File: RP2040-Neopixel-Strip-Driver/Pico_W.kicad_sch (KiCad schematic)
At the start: 1 part

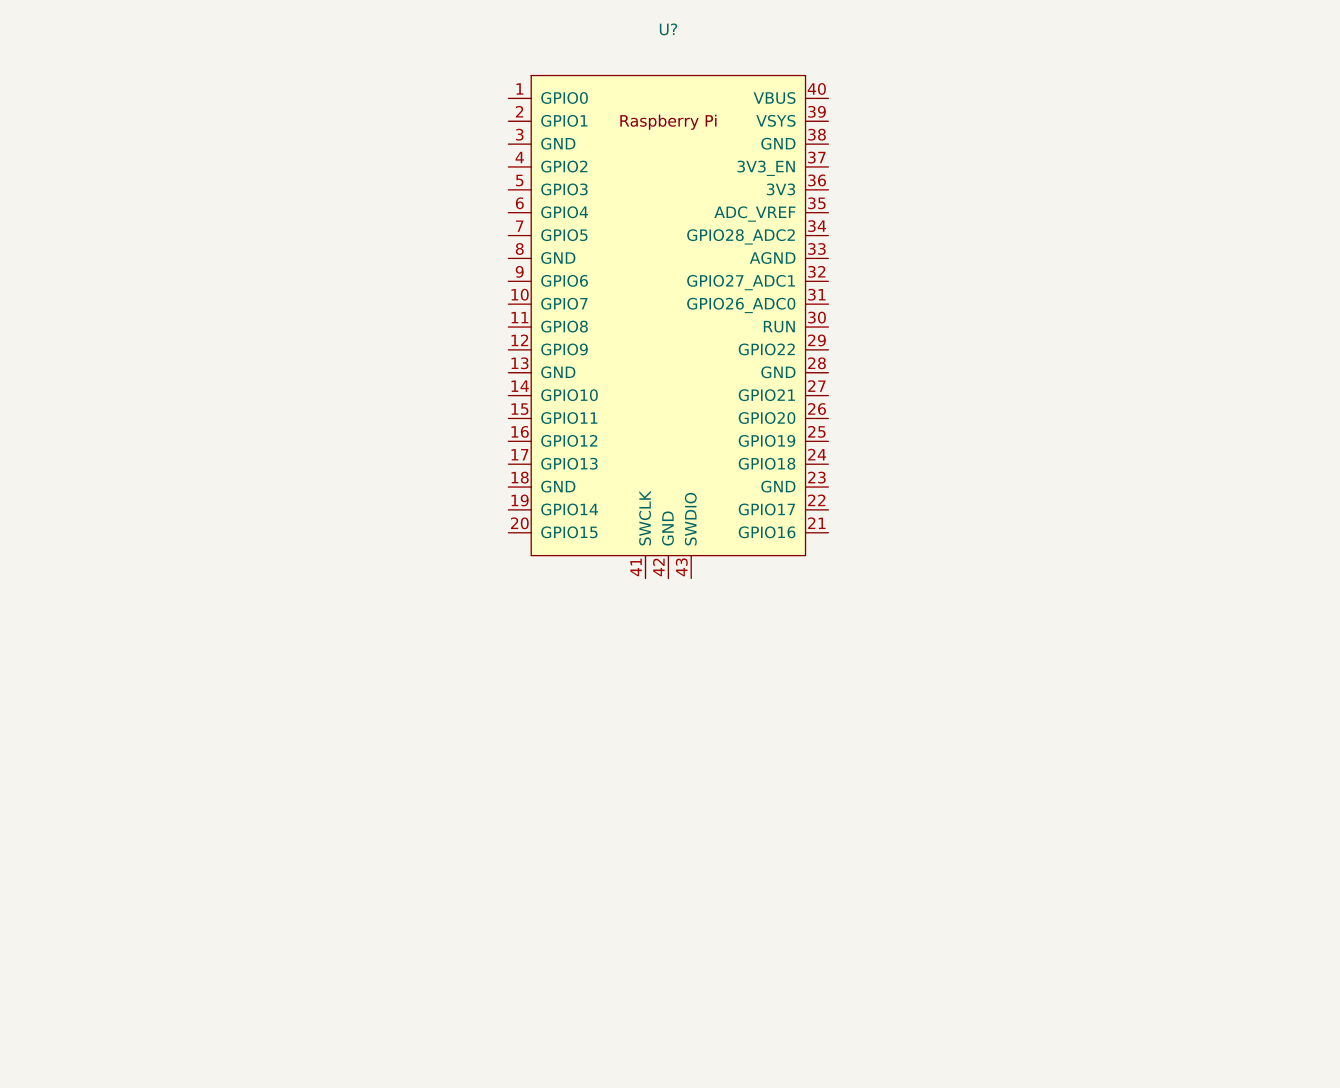
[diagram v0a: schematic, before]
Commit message: Removed RP2040 Schematic, Going with Pico W Module
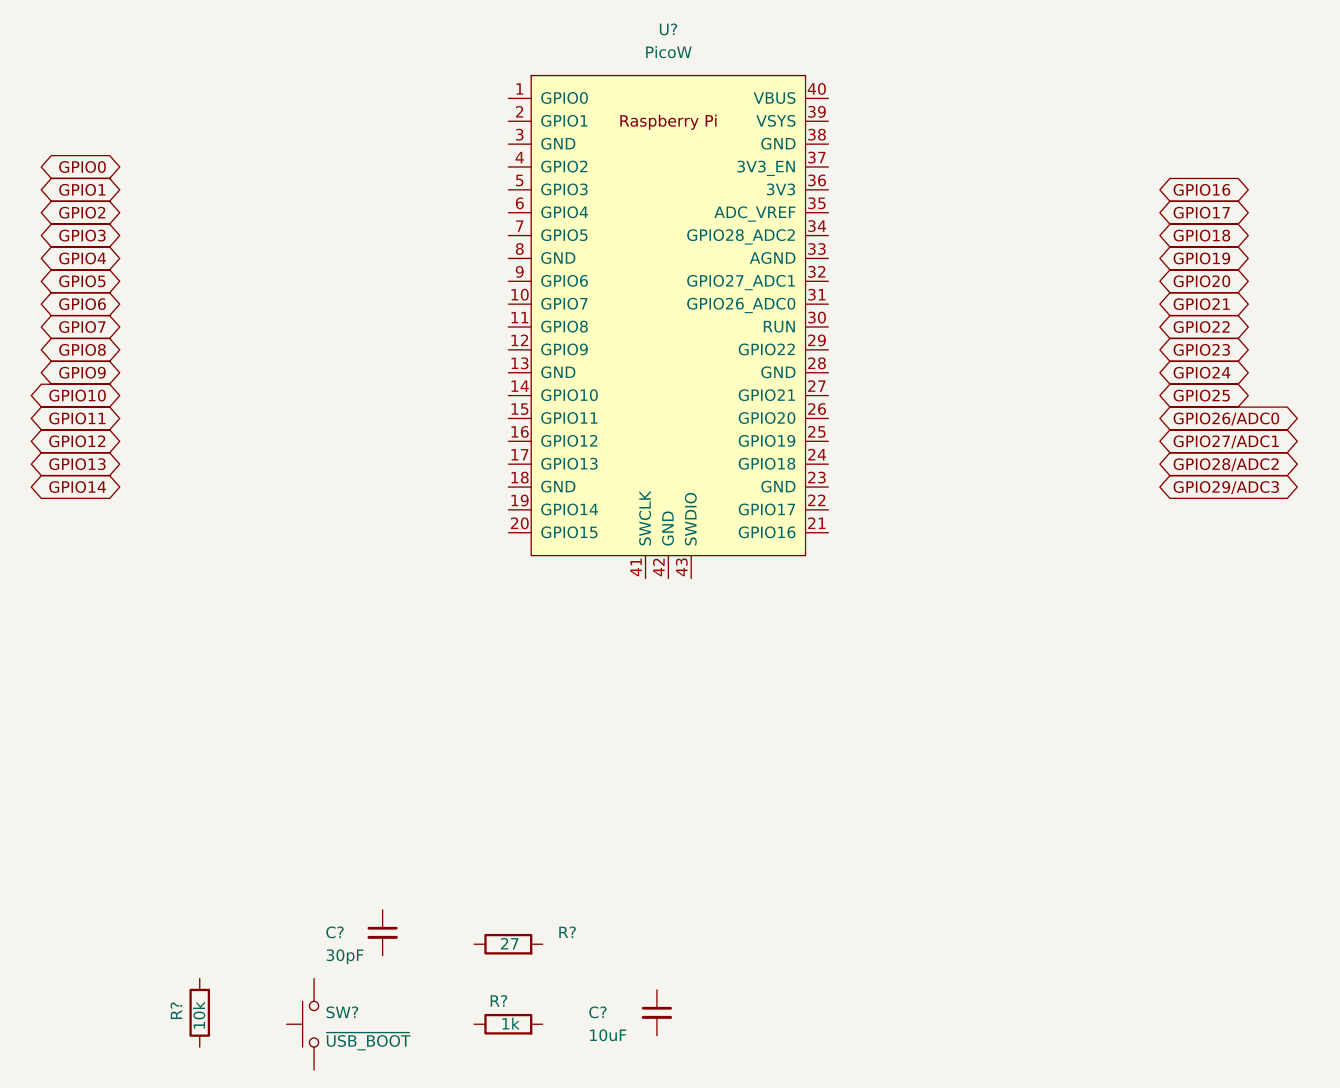
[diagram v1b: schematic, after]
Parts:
- added C?: 10uF, Breadstick Footprints:Perfect_0402_Cap, symbol Device:C_Small
- added C?: 30pF, Breadstick Footprints:Perfect_0402_Cap, symbol Device:C_Small
- added R?: 27, Breadstick Footprints:Perfect_0402_Resistor, symbol Device:R
- added R?: 1k, Breadstick Footprints:Perfect_0402_Resistor, symbol Device:R
- added R?: 10k, Breadstick Footprints:Perfect_0402_Resistor, symbol Device:R
- added SW?: ~{USB_BOOT}, Breadstick Footprints:GT-TC029B-H025-L1N, symbol Switch:SW_Push
- U?: value (none) -> PicoW; footprint (none) -> Pico W:RPi_PicoW_SMD_TH
